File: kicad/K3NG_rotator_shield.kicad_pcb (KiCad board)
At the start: 2 copper layers, 68.6 x 53.3 mm, 8 parts, among them P1 Power, P2 Analog, P3 Digital, P4 Digital, P5 CONN_01X01, P6 CONN_01X01, P7 CONN_01X01, P8 CONN_01X01

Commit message: Ready for final proofread
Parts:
- added C1: .01u, Capacitor_THT:C_Disc_D4.3mm_W1.9mm_P5.00mm, F.Cu at (154.2, 105.5)
- added C2: .01u, Capacitor_THT:C_Disc_D4.3mm_W1.9mm_P5.00mm, F.Cu at (154.2, 100.5)
- added C3: .01u, Capacitor_THT:C_Disc_D4.3mm_W1.9mm_P5.00mm, F.Cu at (154.2, 96.9)
- added C4: 10u, Capacitor_THT:CP_Radial_D4.0mm_P2.00mm, F.Cu at (145.5, 103.0)
- added J1: Screw_Terminal_01x06, SamacSys_Parts:1725698, F.Cu at (165.9, 97.9)
- added P8: CONN_01X01, Socket_Arduino_Uno:Arduino_1pin, F.Cu at (177.0, 108.1)
- added P8: CONN_01X01, Socket_Arduino_Uno:Arduino_1pin, F.Cu at (177.0, 100.5)
- added Q1: 2N2222Ae3, SamacSys_Parts:JANTX2N2222A, F.Cu at (151.6, 89.8)
- added Q2: 2N2222Ae3, SamacSys_Parts:JANTX2N2222A, F.Cu at (160.3, 89.8)
- added R1: 1k, Resistor_THT:R_Axial_DIN0204_L3.6mm_D1.6mm_P5.08mm_Horizontal, F.Cu at (161.8, 120.3)
- added R2: 1k, Resistor_THT:R_Axial_DIN0204_L3.6mm_D1.6mm_P5.08mm_Horizontal, F.Cu at (156.7, 79.1)
- added R3: 4k7, Resistor_THT:R_Axial_DIN0204_L3.6mm_D1.6mm_P5.08mm_Horizontal, F.Cu at (152.7, 81.2)
- added R4: 1k, Resistor_THT:R_Axial_DIN0204_L3.6mm_D1.6mm_P5.08mm_Horizontal, F.Cu at (159.3, 79.1)
- added SW1: SW_Push_Dual, Button_Switch_THT:SW_PUSH_6mm_H4.3mm, F.Cu at (144.0, 117.2)
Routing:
- net /SPDctlr: track 0.00 -> 44.0 mm
- net /CCWctlr: track 0.00 -> 20.7 mm
- net /AZctlr: track 0.00 -> 17.4 mm
- net /CWctlr: track 0.00 -> 13.4 mm
- net /Reset: track 0.00 -> 13.1 mm
- net Net-(Q1-Pad2): track 0.00 -> 10.1 mm
- net /8: track 0.00 -> 5.59 mm
- net Net-(Q2-Pad2): track 0.00 -> 4.74 mm
- net /A0: track 0.00 -> 3.56 mm
- net /7: track 0.00 -> 3.56 mm
- net /6(**): track 0.00 -> 3.56 mm
- added copper zone on B.Cu, net GND
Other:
- board text added: "AZ"
- board text added: "Arduino Reset"
- board text added: "CCW"
- board text added: "CW"
- board text added: "GND"
- board text added: "K3NG Rotator Controller Basic AZ Interface For Yaesu G-800DXA Designed by KQ9P"
- board text added: "NC"
- board text added: "SPD"

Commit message: Part selection and layout complete
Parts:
- removed SW1: SW_Push_Dual, Button_Switch_THT:SW_PUSH_6mm_H4.3mm
- added S1: D6C40F2LFS, SamacSys_Parts:D6C40F2LFS, F.Cu at (122.7, 110.1)
- C1, C2, C3: value .01u -> RDER71H103K0M1H03A; footprint Capacitor_THT:C_Disc_D4.3mm_W1.9mm_P5.00mm -> SamacSys_Parts:RCE5C1H103J1A2H03B
- C4: value 10u -> EEA-GA1E100B; footprint Capacitor_THT:CP_Radial_D4.0mm_P2.00mm -> SamacSys_Parts:CAPPRD150W50D400H800
- Q1, Q2: value 2N2222Ae3 -> 2N2222A; footprint SamacSys_Parts:JANTX2N2222A -> SamacSys_Parts:TO-18_4
- R1, R2, R4: value 1k -> CFM14JT1K00; footprint Resistor_THT:R_Axial_DIN0204_L3.6mm_D1.6mm_P5.08mm_Horizontal -> CFM14JT1K0:CFM14JT1K00
- R3: value 4k7 -> CFM14JT4K70; footprint Resistor_THT:R_Axial_DIN0204_L3.6mm_D1.6mm_P5.08mm_Horizontal -> CFM14JT4K70:CFM14JT4K70
- moved Q1 26.1 mm to (130.8, 105.5), turned to 90 degrees
- moved Q2 25.9 mm to (135.6, 97.9), turned to 90 degrees
- moved R4 18.8 mm to (144.5, 90.8), turned to 0 degrees
- moved R2 14.1 mm to (144.5, 86.2), turned to 0 degrees
- moved C3 11.2 mm to (143.0, 97.9), turned to 270 degrees
- moved R3 9.16 mm to (161.8, 81.7)
- moved C4 7.77 mm to (153.2, 104.5), turned to 90 degrees
- moved C2 6.60 mm to (148.1, 103.0), turned to 90 degrees
- moved C1 4.66 mm to (158.2, 107.8), turned to 90 degrees
- turned R1 to 180 degrees
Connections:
- C1 pad 1: GND -> /AZctlr
- C1 pad 2: /AZctlr -> GND
- C3 pad 1: GND -> /CWctlr
- C3 pad 2: /CWctlr -> GND
- C4 pad 1: /SPDctlr -> GND
- C4 pad 2: GND -> /SPDctlr
- P2 pad 5: /A4(SDA) -> Net-(P2-Pad5)
- P2 pad 6: /A5(SCL) -> Net-(P2-Pad6)
- P3 pad 1: /A5(SCL) -> Net-(P3-Pad1)
- P3 pad 2: /A4(SDA) -> Net-(P3-Pad2)
- Q1 pad 1: GND -> Net-(Q1-Pad1)
- Q1 pad 2: Net-(Q1-Pad2) -> GND
- Q2 pad 1: GND -> Net-(Q2-Pad1)
- Q2 pad 2: Net-(Q2-Pad2) -> GND
- R2 pad 1: /7 -> Net-(Q1-Pad1)
- R2 pad 2: Net-(Q1-Pad2) -> /7
- R3 pad 1: /8 -> /SPDctlr
- R3 pad 2: /SPDctlr -> /8
- R4 pad 1: /6(**) -> Net-(Q2-Pad1)
- R4 pad 2: Net-(Q2-Pad2) -> /6(**)
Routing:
- net /SPDctlr: track 44.0 -> 12.7 mm
- net Net-(Q1-Pad1): track 0.00 -> 28.8 mm
- net /Reset: track 13.1 -> 29.9 mm
- net /CWctlr: track 13.4 -> 29.0 mm
- net /CCWctlr: track 20.7 -> 35.9 mm
- net /6(**): track 3.56 -> 18.1 mm
- net Net-(Q2-Pad1): track 0.00 -> 11.3 mm
- net Net-(Q1-Pad2): track 10.1 -> 0.00 mm
- net /7: track 3.56 -> 12.5 mm
- net /AZctlr: track 17.4 -> 22.8 mm
- net Net-(Q2-Pad2): track 4.74 -> 0.00 mm
- net /8: track 5.59 -> 6.62 mm
- added copper zone on F.Cu, net GND

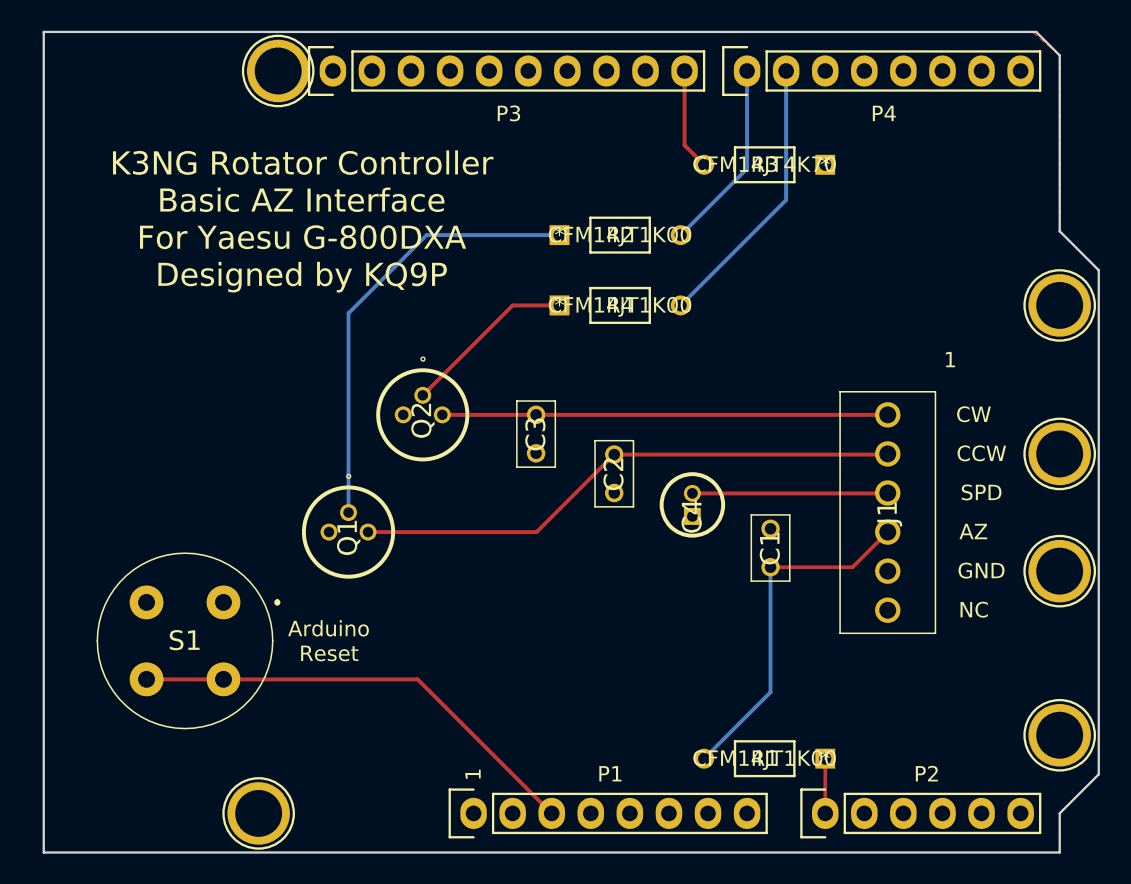
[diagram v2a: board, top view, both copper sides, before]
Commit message: Fixed mistakes, generated Gerbers, ordered
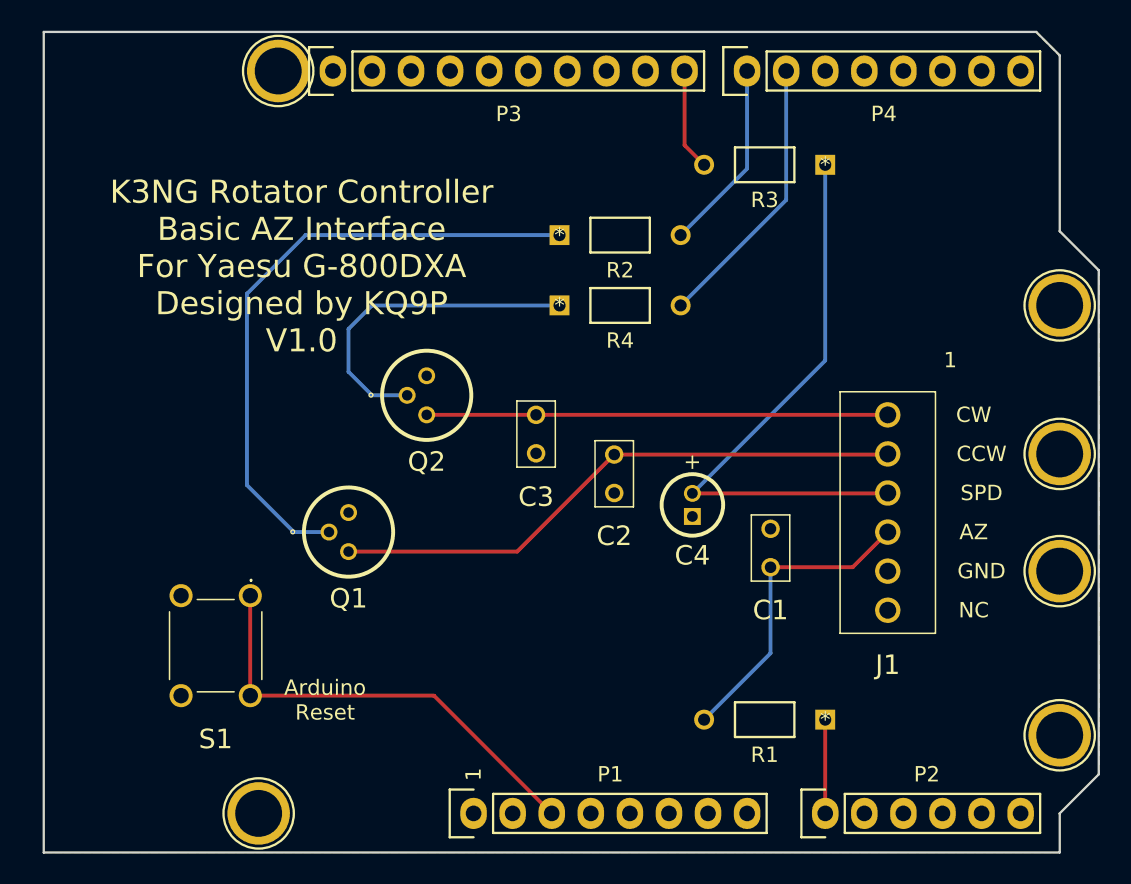
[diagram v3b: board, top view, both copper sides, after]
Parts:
- S1: value D6C40F2LFS -> 1825967-2; footprint SamacSys_Parts:D6C40F2LFS -> SamacSys_Parts:18259672
- moved R1 2.54 mm to (161.8, 117.7)
- moved S1 2.34 mm to (122.2, 112.4)
- moved Q2 1.30 mm to (135.9, 96.6), turned to 180 degrees
- turned Q1 to 180 degrees
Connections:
- Q1 pad 2: GND -> /CCWctlr
- Q1 pad 3: /CCWctlr -> GND
- Q2 pad 2: GND -> /CWctlr
- Q2 pad 3: /CWctlr -> GND
- S1 pad 1: GND -> /Reset
- S1 pad 2: GND -> /Reset
- S1 pad 3: /Reset -> GND
- S1 pad 4: /Reset -> GND
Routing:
- net /SPDctlr: track 12.7 -> 37.6 mm
- net Net-(Q1-Pad1): track 28.8 -> 40.9 mm
- net Net-(Q2-Pad1): track 11.3 -> 21.6 mm
- net /AZctlr: track 22.8 -> 20.3 mm
- net /A0: track 3.56 -> 6.10 mm
- net /CCWctlr: track 35.9 -> 37.7 mm
- net /CWctlr: track 29.0 -> 30.0 mm
- net /Reset: track 29.9 -> 29.3 mm
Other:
- board text added: "+"
- board text added: "Basic AZ Interface V1.0"
- board text added: "K3NG Rotator Controller Basic AZ Interface For Yaesu G-800DXA Designed by KQ9P V1.0"
- board text removed: "K3NG Rotator Controller Basic AZ Interface For Yaesu G-800DXA Designed by KQ9P"
